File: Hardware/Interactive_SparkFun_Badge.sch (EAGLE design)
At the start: 30 parts, among them J1 AVR_SPI_PRG_6PTH, U1 ATMEGA328P

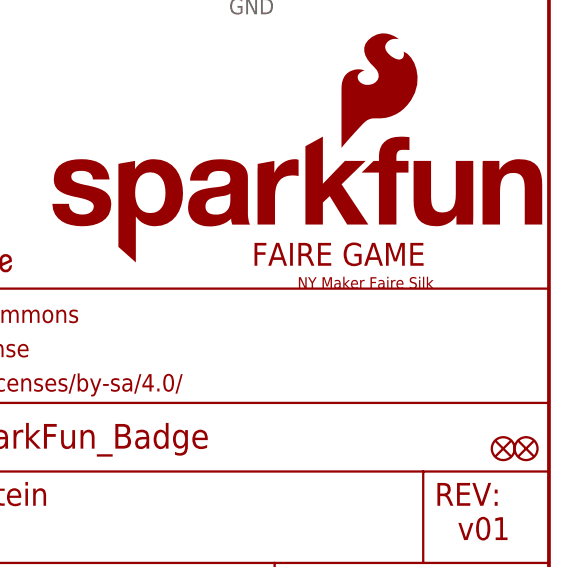
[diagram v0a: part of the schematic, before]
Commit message: Adding Rome MF back silk
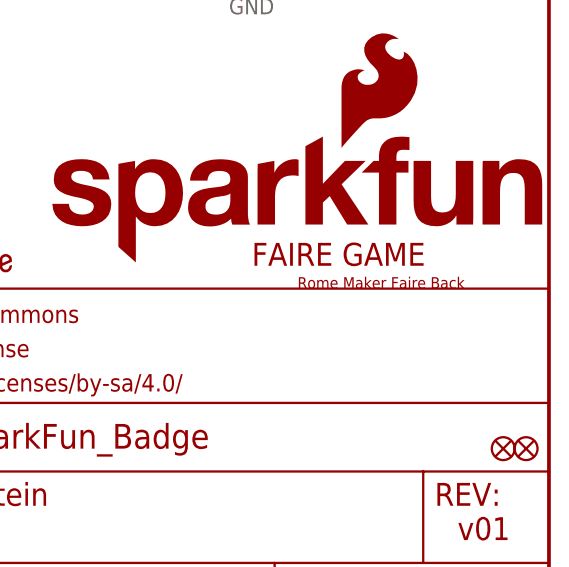
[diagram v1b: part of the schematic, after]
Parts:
- U$2: value NY_FAIRE_BACK -> ROME_FAIRE_BACK; device Local Library:NY_FAIRE_BACK -> Local Library:ROME_FAIRE_BACK
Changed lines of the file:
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@@
 <part name="S2" library="SparkFun-Electromechanical" deviceset="SWITCH-SPDT" device="SMD"/>
 <part name="U$4" library="Local Library" deviceset="FAIRE_GAME_SILK" device=""/>
-<part name="U$2" library="Local Library" deviceset="NY_FAIRE_BACK" device=""/>
+<part name="U$2" library="Local Library" deviceset="ROME_FAIRE_BACK" device=""/>
 </parts>
 <sheets>
